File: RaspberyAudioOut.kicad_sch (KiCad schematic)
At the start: 14 parts

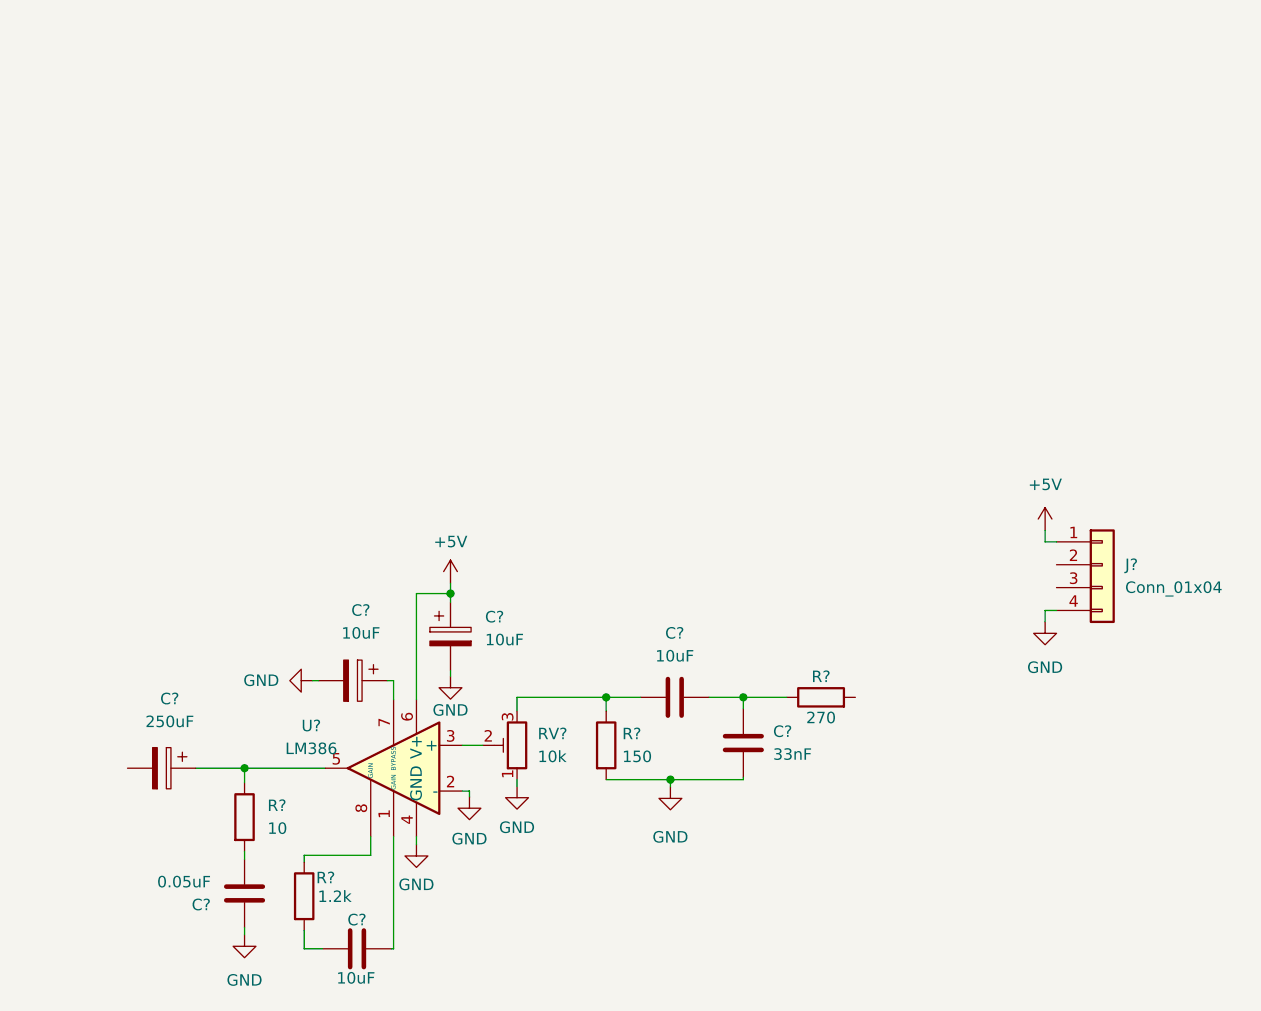
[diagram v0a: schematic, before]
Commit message: Finished PCB step1
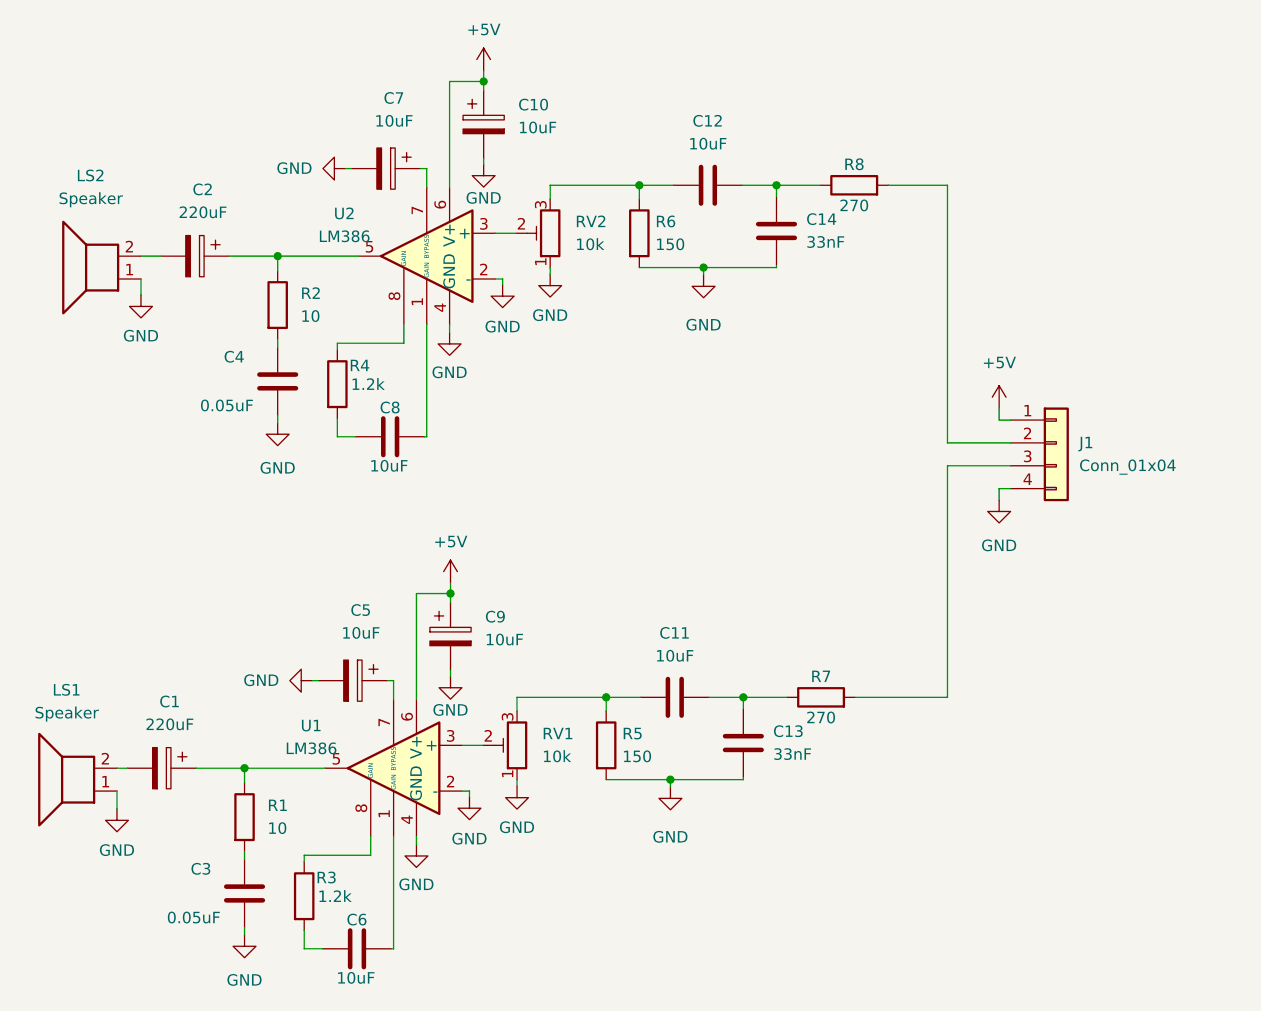
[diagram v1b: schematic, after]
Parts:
- added C10, C7: 10uF, Capacitor_SMD:CP_Elec_5x5.4, symbol Device:C_Polarized
- added C12, C8: 10uF, Capacitor_SMD:C_1206_3216Metric, symbol Device:C
- added C14: 33nF, Capacitor_SMD:C_1206_3216Metric, symbol Device:C
- added C2: 220uF, Capacitor_Tantalum_SMD:CP_EIA-6032-28_Kemet-C_Pad2.25x2.35mm_HandSolder, symbol Device:C_Polarized
- added C4: 0.05uF, Capacitor_SMD:C_1206_3216Metric, symbol Device:C
- added LS1, LS2: Speaker, Connector_PinHeader_1.27mm:PinHeader_2x01_P1.27mm_Vertical_SMD, symbol Device:Speaker
- added R2: 10, Resistor_SMD:R_0805_2012Metric, symbol Device:R
- added R4: 1.2k, Resistor_SMD:R_0805_2012Metric, symbol Device:R
- added R6: 150, Resistor_SMD:R_0805_2012Metric, symbol Device:R
- added R8: 270, Resistor_SMD:R_0805_2012Metric, symbol Device:R
- added RV2: 10k, Potentiometer_THT:Potentiometer_Bourns_3386P_Vertical, symbol Device:R_Potentiometer_Trim
- added U2: LM386, LM386:SOIC127P600X175-8N, symbol Amplifier_Audio:LM386
- C1: renamed from C?; value 250uF -> 220uF; footprint (none) -> Capacitor_Tantalum_SMD:CP_EIA-6032-28_Kemet-C_Pad2.25x2.35mm_HandSolder
- C11, C13, C3, C6: renamed from C?; footprint (none) -> Capacitor_SMD:C_1206_3216Metric
- C5, C9: renamed from C?; footprint (none) -> Capacitor_SMD:CP_Elec_5x5.4
- J1: renamed from J?; footprint Connector_PinHeader_2.00mm:PinHeader_1x02_P2.00mm_Vertical -> Connector_PinHeader_2.54mm:PinHeader_2x02_P2.54mm_Vertical_SMD
- RV1: renamed from RV?; footprint (none) -> Potentiometer_THT:Potentiometer_Bourns_3386P_Vertical
- U1: renamed from U?; footprint (none) -> LM386:SOIC127P600X175-8N
- gave numbers to parts that had none: 4
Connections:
- net +5V: now also C10.1, U2.6 (V+)
- net GND: now also C10.2, C14.2, C4.1, C7.2, LS1.1, LS2.1, R6.2, RV2.1, U2.2 (-), U2.4 (GND)
- net at R7.2: now also J1.3 (Pin_3)
- net at J1.2 (Pin_2): now also R8.2
- net at C1.2: now also LS1.2
- new net: R4.1, U2.8 (GAIN)
- new net: C8.1, R4.2
- new net: C8.2, U2.1 (GAIN)
- new net: RV2.2, U2.3 (+)
- new net: C2.1, R2.1, U2.5
- new net: C7.1, U2.7 (BYPASS)
- new net: C2.2, LS2.2
- new net: C12.1, R6.1, RV2.3
- new net: C12.2, C14.1, R8.1
- new net: C4.2, R2.2
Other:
- moved on the sheet: J1

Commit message: Second step. Changed traces width and some components were added
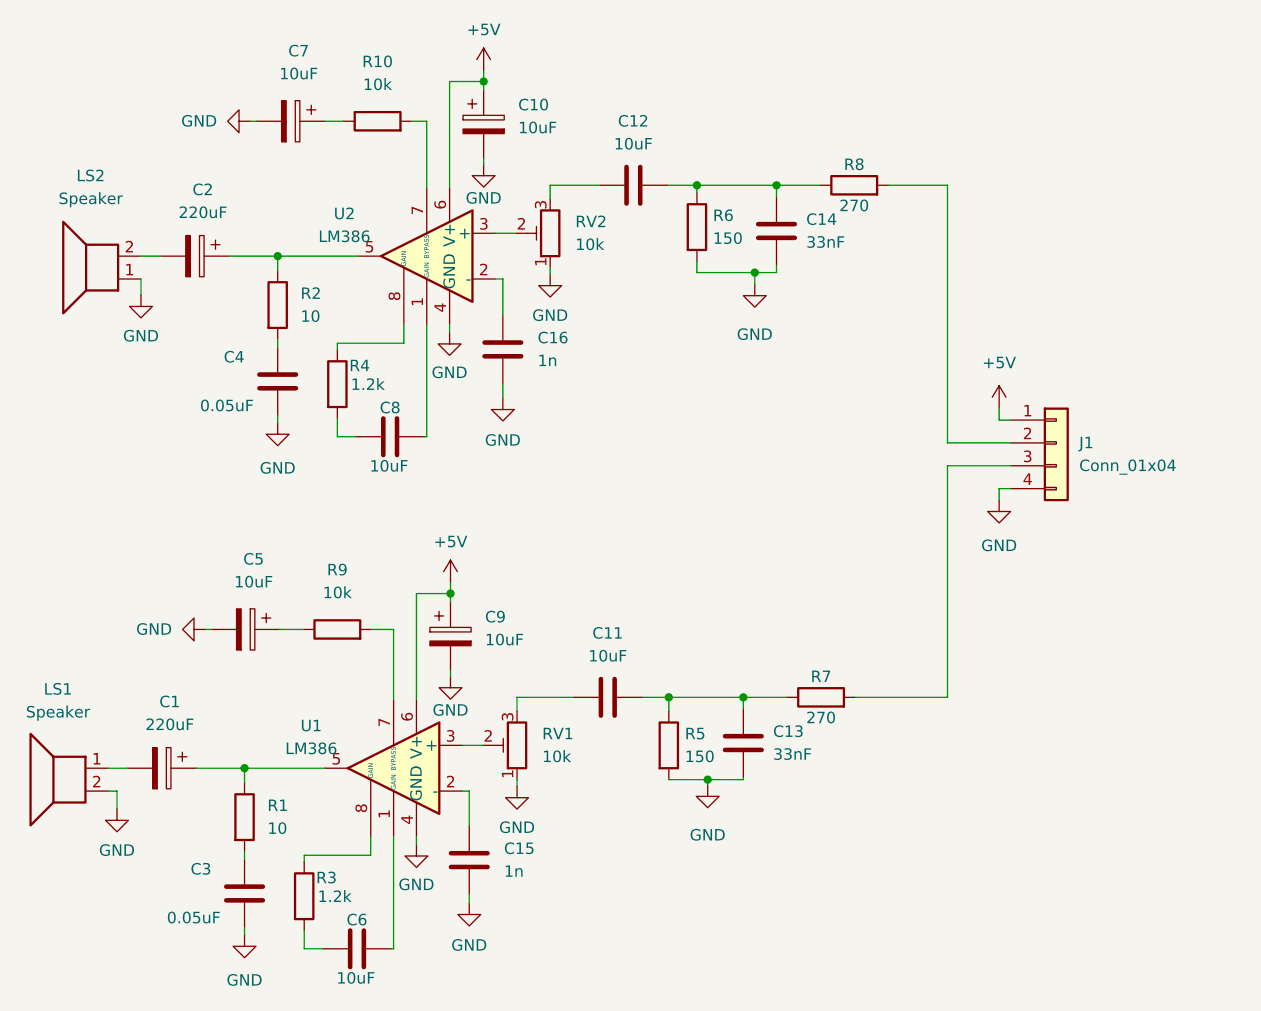
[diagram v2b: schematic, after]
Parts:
- added C15, C16: 1n, Capacitor_SMD:C_0805_2012Metric, symbol Device:C
- added R10, R9: 10k, Resistor_SMD:R_0805_2012Metric, symbol Device:R
- C13, C14: footprint Capacitor_SMD:C_1206_3216Metric -> Capacitor_SMD:C_0805_2012Metric
- J1: footprint Connector_PinHeader_2.54mm:PinHeader_2x02_P2.54mm_Vertical_SMD -> Connector_PinHeader_2.54mm:PinHeader_2x02_P2.54mm_Vertical
- LS1, LS2: footprint Connector_PinHeader_1.27mm:PinHeader_2x01_P1.27mm_Vertical_SMD -> Connector_PinSocket_2.54mm:PinSocket_1x02_P2.54mm_Horizontal
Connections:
- net GND: now also LS1.2, C15.2, C16.2; no longer LS1.1, U1.2 (-), U2.2 (-)
- net at U2.7 (BYPASS): now also R10.2; no longer C7.1
- net at C11.2, C13.1, R7.1: now also R5.1
- net at C11.1, RV1.3: no longer R5.1
- net at C12.1, RV2.3: no longer R6.1
- net at C12.2, C14.1, R8.1: now also R6.1
- net at C1.2: now also LS1.1; no longer LS1.2
- net at U1.7 (BYPASS): now also R9.2; no longer C5.1
- new net: C16.1, U2.2 (-)
- new net: C7.1, R10.1
- new net: C15.1, U1.2 (-)
- new net: C5.1, R9.1
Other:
- moved on the sheet: C11, C12, C5, C7, LS1, R5, R6

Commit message: Changed tantal to electrolitic output capacitor
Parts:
- added R11, R12: 0, Resistor_SMD:R_1206_3216Metric_Pad1.30x1.75mm_HandSolder, symbol Device:R
- C1, C2: value 220uF -> 1000uF; footprint Capacitor_Tantalum_SMD:CP_EIA-6032-28_Kemet-C_Pad2.25x2.35mm_HandSolder -> Capacitor_SMD:CP_Elec_10x10.5
- J1: footprint Connector_PinHeader_2.54mm:PinHeader_2x02_P2.54mm_Vertical -> Connector_PinHeader_2.54mm:PinHeader_1x04_P2.54mm_Vertical
- U1, U2: footprint LM386:SOIC127P600X175-8N -> LM386MX-1_NOPB:SOIC127P600X175-8N
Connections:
- net GND: now also LS1.1, R1.2, R2.2; no longer C3.1, C4.1, LS1.2
- net at C2.1, U2.5: now also C4.2; no longer R2.1
- net at R7.2: now also R12.2; no longer J1.3 (Pin_3)
- net at C3.2: now also C1.1, U1.5; no longer R1.2
- net at R8.2: now also R11.1; no longer J1.2 (Pin_2)
- net at C1.2: now also LS1.2; no longer LS1.1
- new net: C3.1, R1.1
- new net: J1.2 (Pin_2), R11.2
- new net: J1.3 (Pin_3), R12.1
- new net: C4.1, R2.1
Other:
- moved on the sheet: C3, C4, LS1, R1, R2
